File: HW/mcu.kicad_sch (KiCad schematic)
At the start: 2 parts

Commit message: Fixed board, big work in schematic, to finish
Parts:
- removed TH?: (no value), symbol Device:Thermistor_NTC
- added C7, C8: (no value), symbol Device:C_Small
- added C9: 100n, symbol Device:C_Small
- added D2: (no value), symbol Device:LED
- added D3: (no value), symbol Power_Protection:PRTR5V0U2X
- added J1: (no value), symbol Connector:USB_C_Receptacle_USB2.0
- added J2: (no value), symbol Connector_Generic:Conn_01x05
- added J3: (no value), symbol Connector_Generic:Conn_01x03
- added R6, R8, R9: (no value), symbol Device:R_Small
- added R7: 5k1, symbol Device:R_Small
- added SW2: (no value), symbol Switch:SW_DPST
- added TP1: (no value), symbol Connector:TestPoint
- U1: renamed from U?; value ESP32-S2-MINI-2 -> (none)
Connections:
- net GND: now reaches U1.1 (GND)
- net GND: now also C7.1, C8.2, C9.2, D2.1 (K), D3.1 (GND), J1.A1 (GND), J1.A12 (GND), J1.B1 (GND), J1.B12 (GND), J2.5 (Pin_5), J3.3 (Pin_3), R6.2, R7.2, SW2.2, SW2.4
- net USB_D-: now reaches U1.23 (USB_D-/ADC2_CH8/GPIO19)
- net USB_D-: now also D3.3 (I/O2), J1.A7 (D-), J1.B7 (D-)
- net USB_D+: now reaches U1.24 (USB_D+/ADC2_CH9/GPIO20)
- net USB_D+: now also D3.2 (I/O1), J1.A6 (D+), J1.B6 (D+)
- net SDA: now reaches U1.28 (GPIO33)
- net SCL: now reaches U1.29 (GPIO34)
- net +3V3: now reaches U1.3 (3V3)
- net +3V3: now also C7.2, C8.1, D3.4 (VCC), R9.1
- net Temp_mosfet: now reaches U1.31 (GPIO35)
- net Temp_heater_3: now reaches U1.32 (GPIO36)
- net Temp_heater_2: now reaches U1.33 (GPIO37)
- net Temp_heater_1: now reaches U1.34 (GPIO38)
- net TCK: now reaches U1.35 (MTCK/JTAG/GPIO39)
- net TCK: now also J2.4 (Pin_4)
- net TDO: now reaches U1.36 (MTDO/JTAG/GPIO40)
- net TDO: now also J2.3 (Pin_3)
- net TDI: now reaches U1.37 (MTDI/JTAG/GPIO41)
- net TDI: now also J2.2 (Pin_2)
- net TMS: now reaches U1.38 (MTMS/JTAG/GPIO42)
- net TMS: now also J2.1 (Pin_1)
- net TX: now reaches U1.39 (GPIO43/U0TXD/PROG)
- net TX: now also J3.1 (Pin_1)
- net RX: now reaches U1.40 (GPIO44/U0RXD/PROG)
- net RX: now also J3.2 (Pin_2)
- net RESET: now reaches U1.45 (CHIP/PU/RESET)
- net RESET: now also C9.1, R9.2, SW2.1, SW2.3
- net current_sense_HIGH: now reaches U1.5 (GPIO1/ADC1_CH0)
- net current_sense_LOW: now reaches U1.6 (GPIO2/ADC1_CH1)
- new net: D2.2 (A), R8.1
- new net: J1.B5 (CC2), R7.1
- new net: J1.A5 (CC1), R6.1
- new net +5V: J1.A4 (VBUS), J1.A9 (VBUS), J1.B4 (VBUS), J1.B9 (VBUS), R8.2, TP1.1
- no-connect marks 0 -> 3
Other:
- note added: "Debug Interfaces"
- note added: "MCU"
- note added: "Reset"
- note added: "USB 1.1 OTG + ESD"
- moved on the sheet: U1

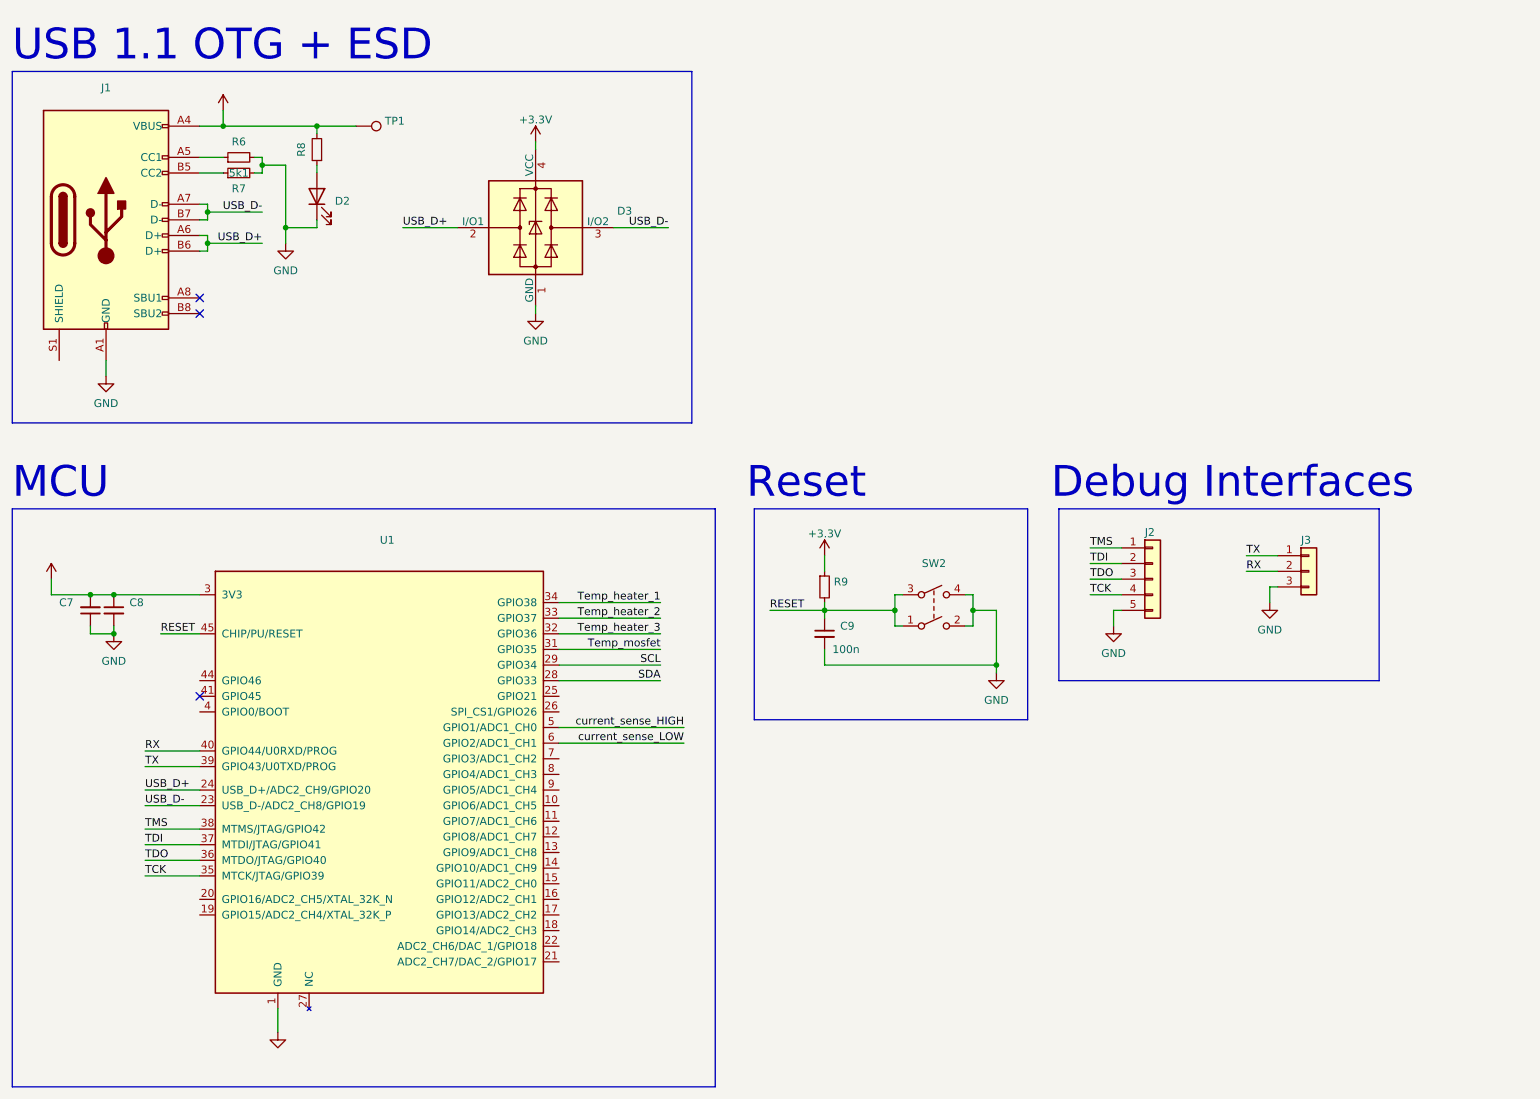
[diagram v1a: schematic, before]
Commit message: Finished sch, to be checked. Initial components layout
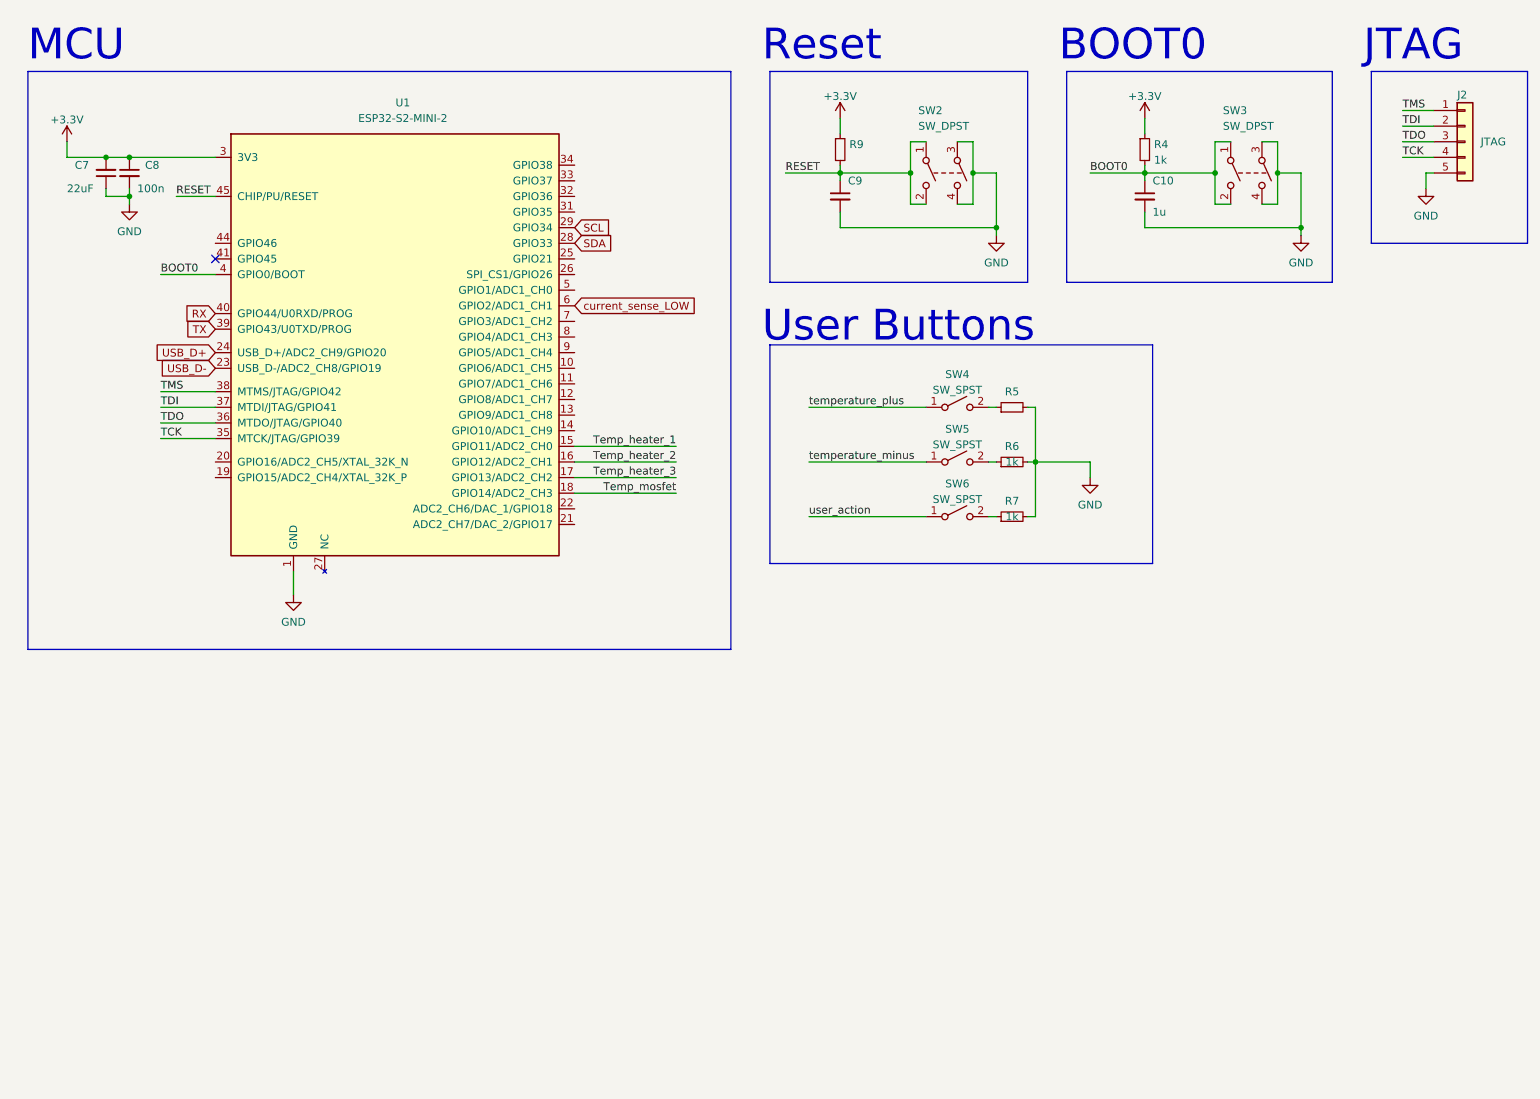
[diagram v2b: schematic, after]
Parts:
- removed D2: (no value), symbol Device:LED
- removed D3: (no value), symbol Power_Protection:PRTR5V0U2X
- removed J1: (no value), symbol Connector:USB_C_Receptacle_USB2.0
- removed J3: (no value), symbol Connector_Generic:Conn_01x03
- removed R8: (no value), symbol Device:R_Small
- removed TP1: (no value), symbol Connector:TestPoint
- added C10: 1u, Capacitor_SMD:C_0603_1608Metric, symbol Device:C_Small
- added R4: 1k, Resistor_SMD:R_0603_1608Metric, symbol Device:R_Small
- added R5: (no value), symbol Device:R_Small
- added SW3: SW_DPST, symbol Switch:SW_DPST
- added SW4, SW5, SW6: SW_SPST, symbol Switch:SW_SPST
- C7: value (none) -> 22uF; footprint (none) -> Capacitor_SMD:C_0603_1608Metric
- C8: value (none) -> 100n; footprint (none) -> Capacitor_SMD:C_0603_1608Metric
- C9: value 100n -> (none); footprint (none) -> Capacitor_SMD:C_0603_1608Metric
- J2: value (none) -> JTAG; footprint (none) -> Connector_PinHeader_2.54mm:PinHeader_1x05_P2.54mm_Vertical
- R6: value (none) -> 1k; footprint (none) -> Resistor_SMD:R_0603_1608Metric
- R7: value 5k1 -> 1k; footprint (none) -> Resistor_SMD:R_0603_1608Metric
- SW2: value (none) -> SW_DPST
- U1: value (none) -> ESP32-S2-MINI-2
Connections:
- net +3V3: now also R4.1
- net GND: now also SW2.3, C10.2, R5.2, SW3.3, SW3.4; no longer SW2.2
- net RESET: now also SW2.2; no longer SW2.3
- net Temp_heater_1: now also U1.15 (GPIO11/ADC2_CH0); no longer U1.34 (GPIO38)
- net Temp_heater_2: now also U1.16 (GPIO12/ADC2_CH1); no longer U1.33 (GPIO37)
- net Temp_heater_3: now also U1.17 (GPIO13/ADC2_CH2); no longer U1.32 (GPIO36)
- net Temp_mosfet: now also U1.18 (GPIO14/ADC2_CH3); no longer U1.31 (GPIO35)
- net BOOT0: now reaches U1.4 (GPIO0/BOOT)
- net BOOT0: now also C10.1, R4.2, SW3.1, SW3.2
- net at R7.1: now also SW6.2 (B)
- net at R6.1: now also SW5.2 (B)
- net current_sense_HIGH: no longer names the net of U1.5 (GPIO1/ADC1_CH0)
- new net: R5.1, SW4.2 (B)
- new net temperature_minus: SW5.1 (A)
- new net temperature_plus: SW4.1 (A)
- new net user_action: SW6.1 (A)
- no-connect marks 3 -> 1
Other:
- note added: "BOOT0"
- note added: "JTAG"
- note added: "User Buttons"
- note removed: "Debug Interfaces"
- note removed: "USB 1.1 OTG + ESD"
- moved on the sheet: C7, C8, C9, J2, R9, SW2, U1

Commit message: Sch finalized, added EMC stuff, user buttons and oled
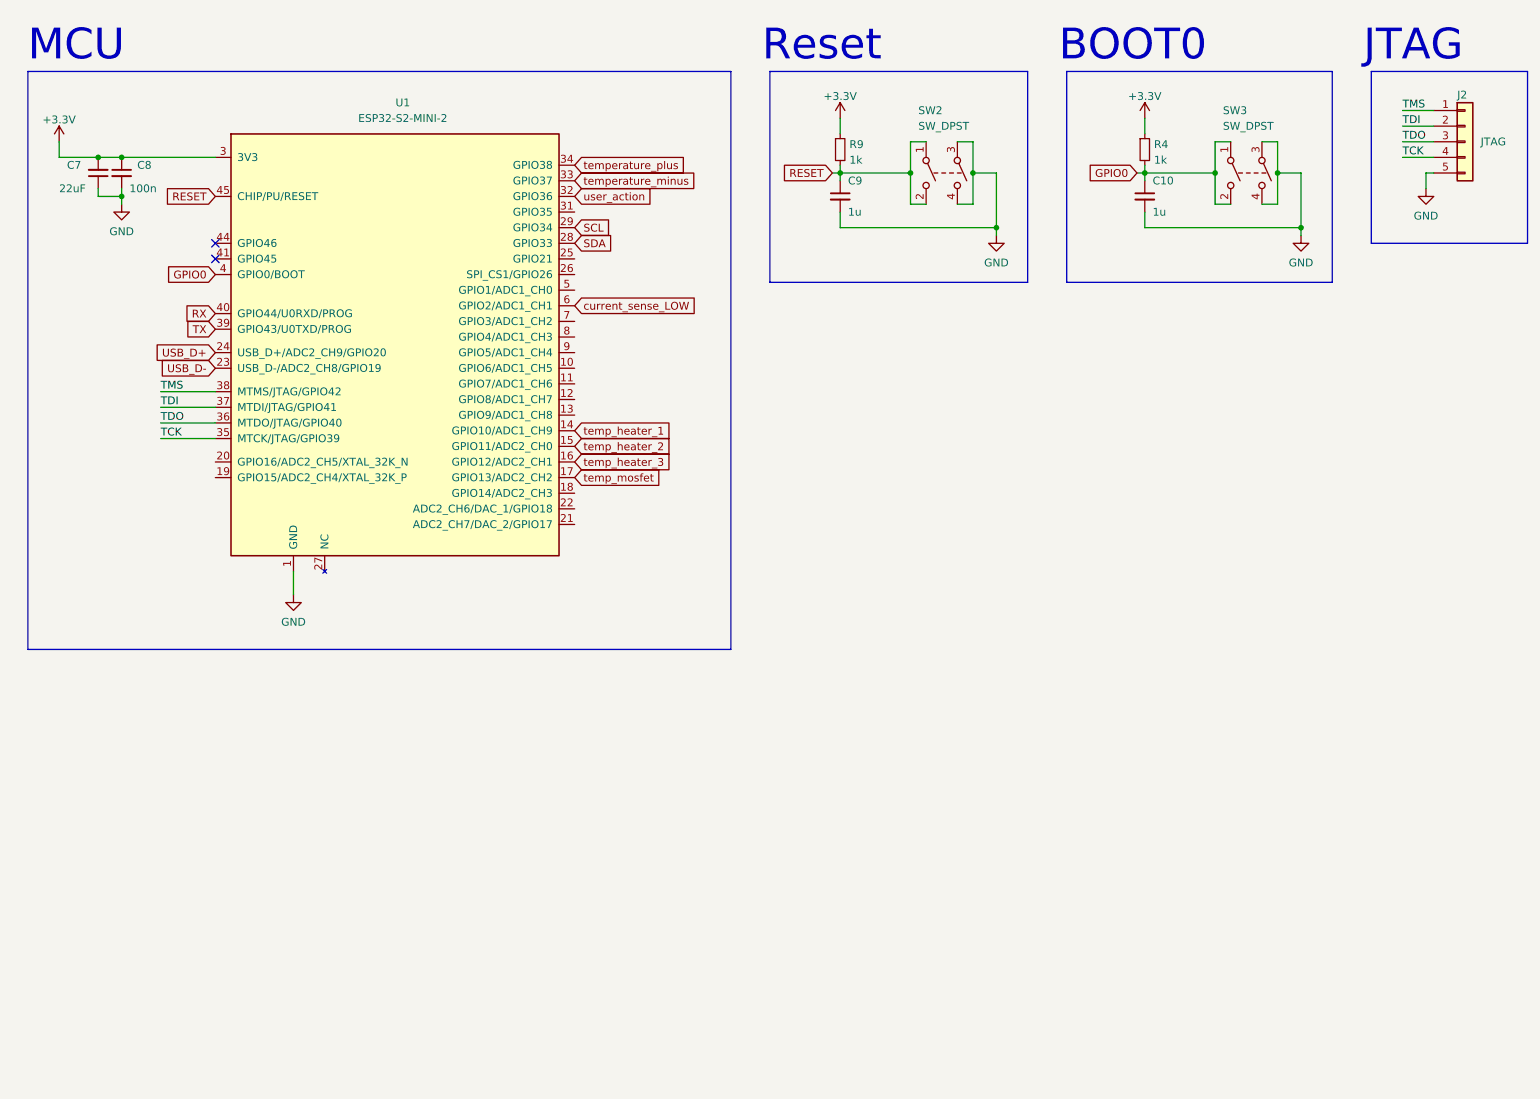
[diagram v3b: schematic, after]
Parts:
- removed R5: (no value), symbol Device:R_Small
- removed R6, R7: 1k, Resistor_SMD:R_0603_1608Metric, symbol Device:R_Small
- removed SW4, SW5, SW6: SW_SPST, symbol Switch:SW_SPST
- C9: value (none) -> 1u
- R9: value (none) -> 1k; footprint (none) -> Resistor_SMD:R_0603_1608Metric
- SW2, SW3: footprint (none) -> SKRPACE010:SW_SKRPACE010
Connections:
- net temperature_minus: now also U1.33 (GPIO37)
- net temperature_plus: now also U1.34 (GPIO38)
- net user_action: now also U1.32 (GPIO36)
- net temp_heater_1: now reaches U1.14 (GPIO10/ADC1_CH9)
- net BOOT0 renamed GPIO0
- net Temp_heater_1 renamed temp_heater_2
- net Temp_heater_2 renamed temp_heater_3
- net Temp_heater_3 renamed temp_mosfet
- net Temp_mosfet: no longer names the net of U1.18 (GPIO14/ADC2_CH3)
- no-connect marks 1 -> 2
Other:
- note removed: "User Buttons"
- moved on the sheet: C7, C8

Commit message: Work on layout, sch fixes, added several 3d models
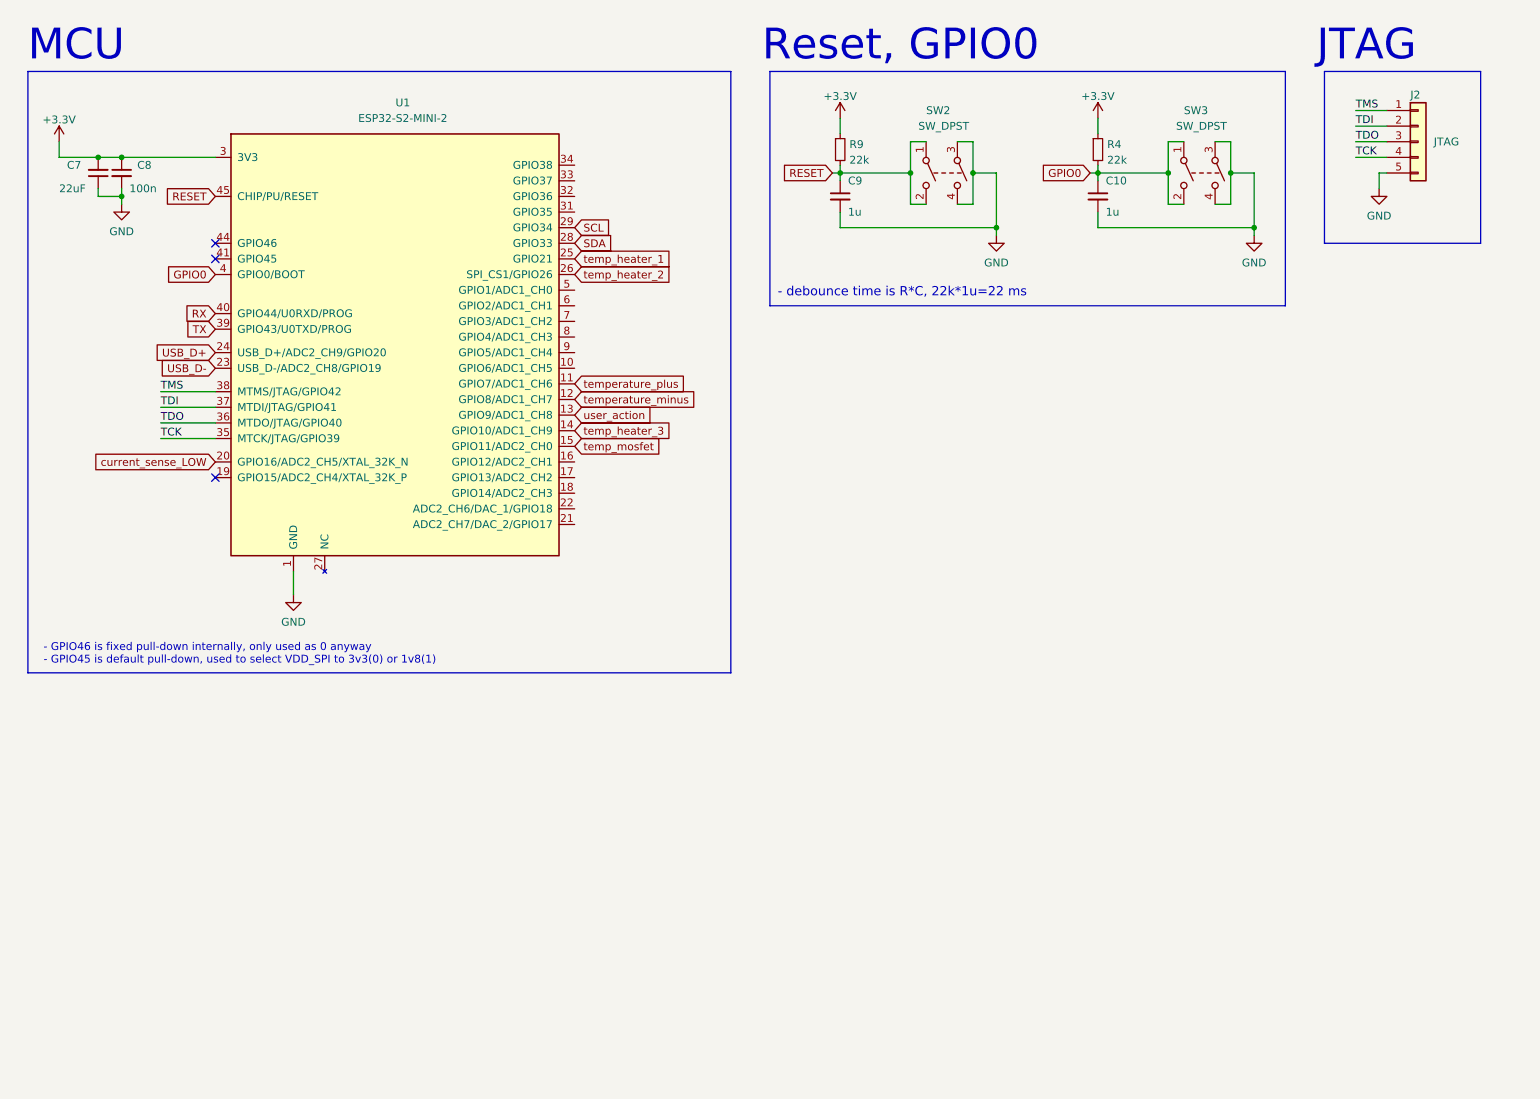
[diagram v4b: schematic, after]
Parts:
- R4, R9: value 1k -> 22k
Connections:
- net current_sense_LOW: now also U1.20 (GPIO16/ADC2_CH5/XTAL_32K_N); no longer U1.6 (GPIO2/ADC1_CH1)
- net temp_heater_1: now also U1.25 (GPIO21); no longer U1.14 (GPIO10/ADC1_CH9)
- net temp_heater_2: now also U1.26 (SPI_CS1/GPIO26); no longer U1.15 (GPIO11/ADC2_CH0)
- net temp_heater_3: now also U1.14 (GPIO10/ADC1_CH9); no longer U1.16 (GPIO12/ADC2_CH1)
- net temp_mosfet: now also U1.15 (GPIO11/ADC2_CH0); no longer U1.17 (GPIO13/ADC2_CH2)
- net temperature_minus: now also U1.12 (GPIO8/ADC1_CH7); no longer U1.33 (GPIO37)
- net temperature_plus: now also U1.11 (GPIO7/ADC1_CH6); no longer U1.34 (GPIO38)
- net user_action: now also U1.13 (GPIO9/ADC1_CH8); no longer U1.32 (GPIO36)
- no-connect marks 2 -> 3
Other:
- note added: "- GPIO46 is fixed pull-down internally, only used as 0 anyway - GPIO45 is default pull-down, used to select VDD_SPI to 3v3(0) or 1v8(1)"
- note added: "- debounce time is R*C, 22k*1u=22 ms"
- note added: "Reset, GPIO0"
- note removed: "BOOT0"
- note removed: "Reset"
- moved on the sheet: C10, J2, R4, SW3
